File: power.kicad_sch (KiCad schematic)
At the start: 31 parts, among them J1 Barrel_Jack_MountingPin, J2 Conn_02x04_Odd_Even, J3 Conn_02x04_Odd_Even, Q1 SI2301CDS-T1-GE3, SW1 Power, U1 TMA-1212D, U2 TPS54302

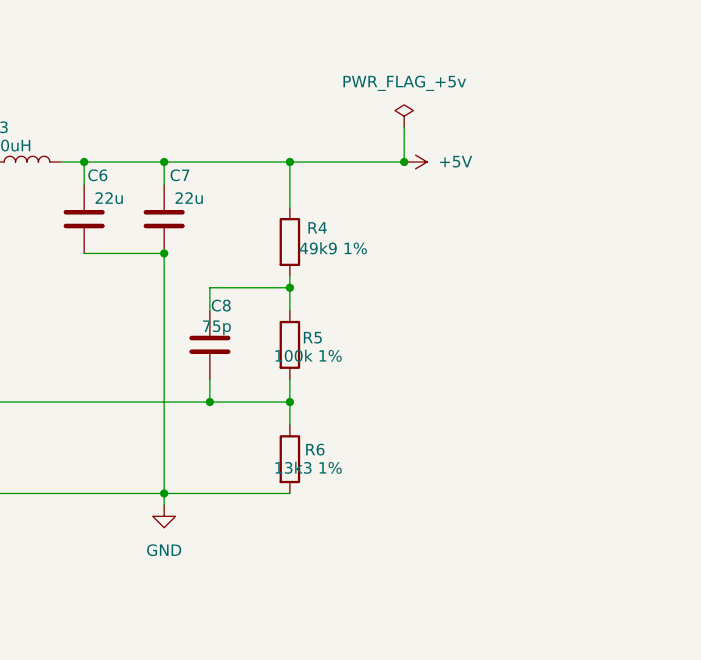
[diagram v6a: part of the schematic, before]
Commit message: add protection to 5v
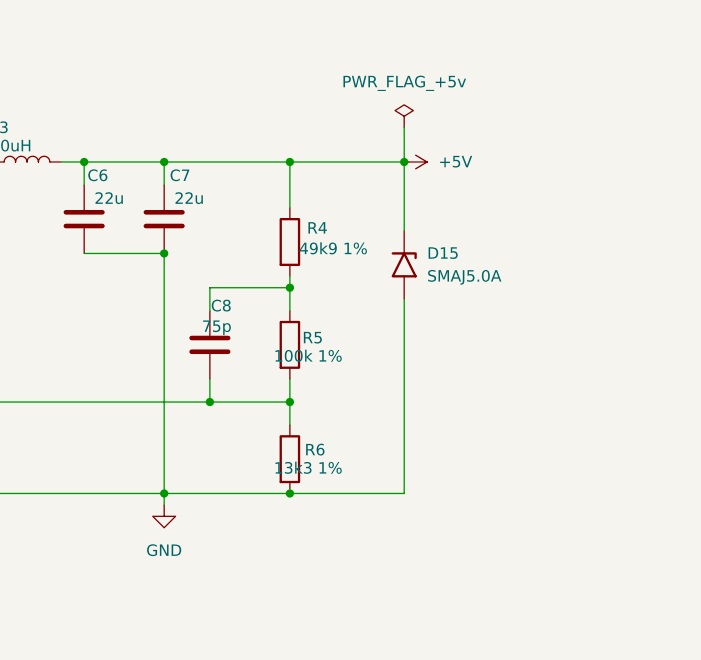
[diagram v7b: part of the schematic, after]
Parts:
- added D15: SMAJ5.0A, Diode_SMD:D_SMA, symbol Diode:SMAJ5.0A
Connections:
- net +5V: now also D15.1 (A1)
- net GND: now also D15.2 (A2)
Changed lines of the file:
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@@
 	)
 	(junction
+		(at 224.79 88.9)
+		(diameter 0)
+		(color 0 0 0 0)
+	)
+	(junction
 		(at 88.9 128.27)
 		(diameter 0)
@@
 	(wire
 		(pts
+			(xy 237.49 67.31) (xy 237.49 88.9)
+		)
+		(stroke
+			(width 0)
+			(type default)
+		)
+	)
+	(wire
+		(pts
 			(xy 231.14 134.62) (xy 231.14 140.97)
 		)
@@
 	(wire
 		(pts
+			(xy 237.49 52.07) (xy 237.49 59.69)
+		)
+		(stroke
+			(width 0)
+			(type default)
+		)
+	)
+	(wire
+		(pts
 			(xy 224.79 78.74) (xy 224.79 81.28)
 		)
@@
 	(wire
 		(pts
+			(xy 237.49 88.9) (xy 224.79 88.9)
+		)
+		(stroke
+			(width 0)
+			(type default)
+		)
+	)
+	(wire
+		(pts
 			(xy 114.3 148.59) (xy 114.3 151.13)
 		)
@@
 					(unit 1)
 				)
+			)
+		)
+	)
+	(symbol
+		(lib_id "Diode:SMAJ5.0A")
+		(at 237.49 63.5 270)
+		(unit 1)
+		(exclude_from_sim no)
+		(in_bom yes)
+		(on_board yes)
+		(dnp no)
+		(fields_autoplaced yes)
+		(property "Reference" "D15"
+			(at 240.03 62.2299 90)
+			(effects
+				(font
+					(size 1.27 1.27)
+				)
+				(justify left)
+			)
+		)
+		(property "Value" "SMAJ5.0A"
+			(at 240.03 64.7699 90)
+			(effects
+				(font
+					(size 1.27 1.27)
+				)
+				(justify left)
+			)
+		)
+		(property "Footprint" "Diode_SMD:D_SMA"
+			(at 232.41 63.5 0)
+			(effects
+				(font
+					(size 1.27 1.27)
+				)
+				(hide yes)
+			)
+		)
+		(property "Datasheet" "https://www.littelfuse.com/media?resourcetype=datasheets&itemid=75e32973-b177-4ee3-a0ff-cedaf1abdb93&filename=smaj-datasheet"
+			(at 237.49 62.23 0)
+			(effects
+				(font
+					(size 1.27 1.27)
+				)
+				(hide yes)
+			)
+		)
+		(property "Description" "400W unidirectional Transient Voltage Suppressor, 5.0Vr, SMA(DO-214AC)"
+			(at 237.49 63.5 0)
+			(effects
+				(font
+					(size 1.27 1.27)
+				)
+				(hide yes)
+			)
+		)
+		(pin "1"
+		)
+		(pin "2"
+		)
+		(instances
+			(project ""
+				(path "/55cca6a8-30da-4c13-b2f2-a01401e2b54c/a1b2c3d4-1111-4000-8000-000000000001"
+					(reference "D15")
+					(unit 1)
+				)

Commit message: update power - still not happy
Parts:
- removed U1: TMA-1212D, Converter_DCDC:Converter_DCDC_TRACO_TMA-05xxD_12xxD_Dual_THT, symbol Converter_DCDC:TMA-1212D
- added PS1: TMR_3-1222E, daisy-studio:TMR1210, symbol daisy-studio:TMR_3-1222E
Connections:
- net +12VA: now also D2.1 (A1); no longer D2.2 (A2)
- net +12V_RAW: now also PS1.2 (+VIN_(VCC))
- net GND: now also D2.2 (A2), PS1.1 (-VIN_(GND)), PS1.3 (REMOTE_ON/OFF), PS1.7 (COMMON); no longer D1.2 (A2), D2.1 (A1), J1.2, R1.2
- net at C2.1, L2.1: now also PS1.6 (+VOUT)
- net at C1.1, L1.1: now also PS1.8 (-VOUT)
- new net: D1.2 (A2), J1.2, R1.2
- no-connect marks 0 -> 2
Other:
- note added: "Physically close to PS1"
- note removed: "Physically close to U1"
- moved on the sheet: C1, C2, C3, C4, D2, D3, L1, L2
